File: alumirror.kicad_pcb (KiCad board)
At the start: 2 copper layers, 139.7 x 87.2 mm, 89 parts, among them J1 USB_C_Receptacle_USB2.0_16P_2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, J2 USB_C_Receptacle_USB2.0_16P_2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, J3 USB_C_Receptacle_USB2.0_16P_2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, J4 USB_C_Receptacle_USB2.0_16P_2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, K00 PG1350, K01 PG1350, K02 PG1350, K03 PG1350, K04 PG1350, K05 PG1350, K10 PG1350, K11 PG1350, K12 PG1350, K13 PG1350, K14 PG1350, K15 PG1350, K20 PG1350, K21 PG1350, K22 PG1350, K23 PG1350, K24 PG1350, K25 PG1350_1½U, K30 PG1350_1½U, K31 PG1350/SKQUCAA010, SW1 BOOT, U1 CH552T, U2 CH552T, U3 USBLC6-2P6, U4 USBLC6-2P6, U5 USBLC6-2P6, U6 USBLC6-2P6

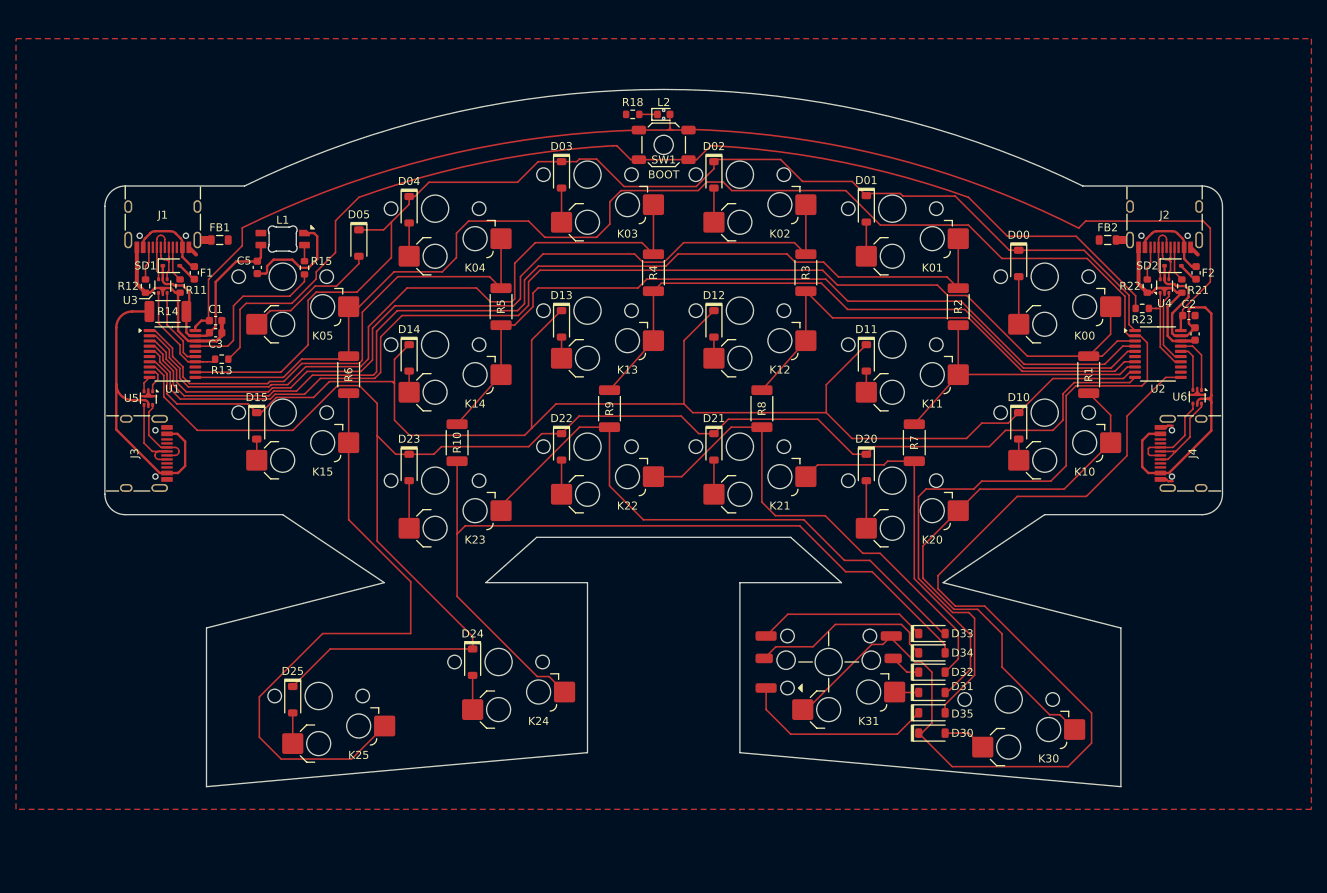
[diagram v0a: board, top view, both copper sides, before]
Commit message: Refine middle layer 3D print cutouts
Also renumber diodes — D0# are now DO# and SD1 and SD2 are and D2
Add diode (D3) on VCC line to RGB LED (this drops VCC to ~4V, which is still within spec., but now closer to the 3.3V control signal as DIN should be VCC±0.5V).
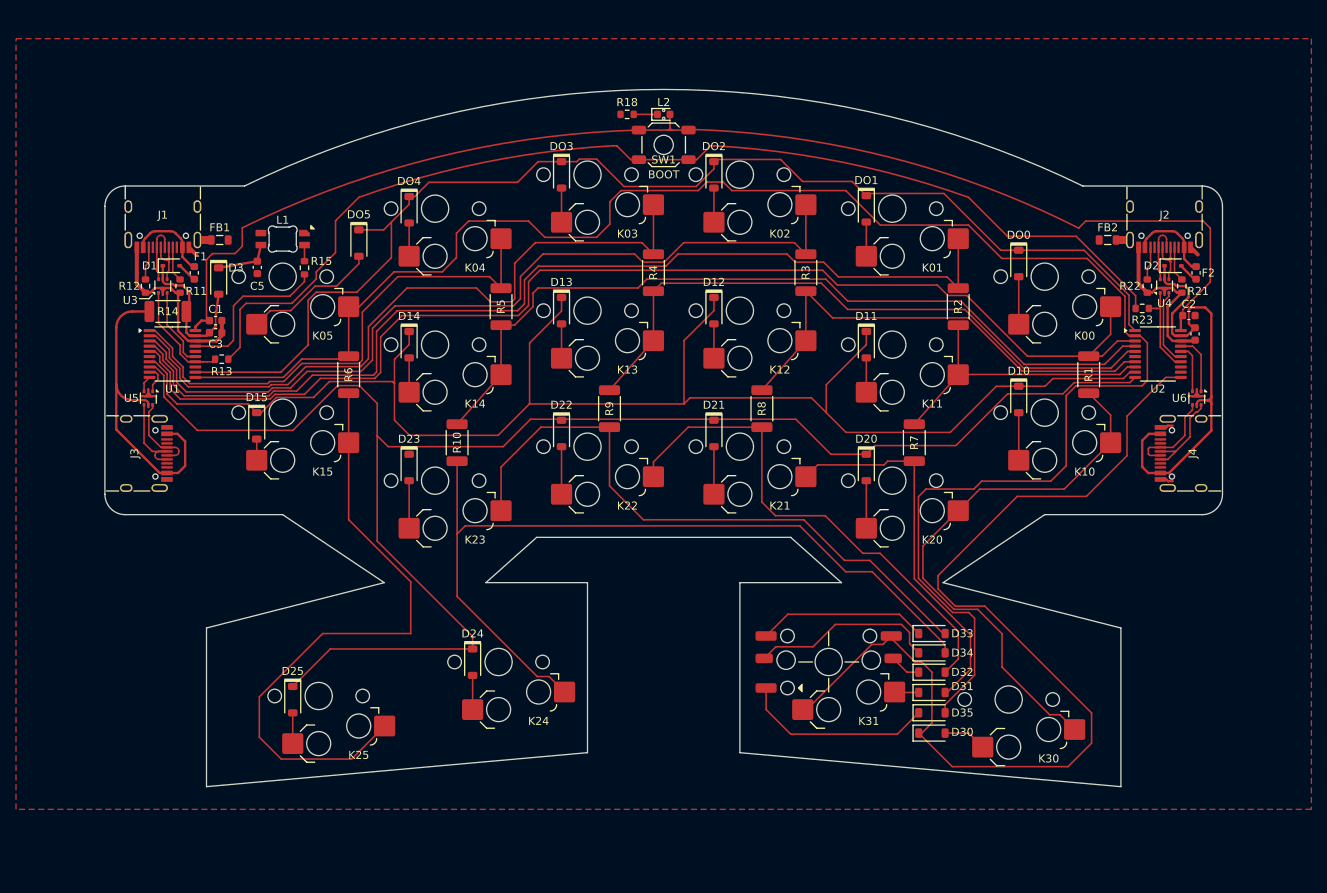
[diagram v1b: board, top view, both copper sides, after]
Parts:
- added D3: 1N4148, Project Library:D_SOD-123_Mod, F.Cu at (96.8, 53.0)
- D30, D31, D32, D33, D34, D35: footprint Project Library:D_SOD-123_Mod -> Diode_SMD:D_SOD-123
- L1: value LED_6028R -> SK6812MINI-E
- R11, R12, R13, R18, R21, R22, R23: footprint Project Library:R_0603_1608Metric_Mod -> Resistor_SMD:R_0603_1608Metric
- R14: footprint Project Library:R_2010_5025Metric_Mod -> Resistor_SMD:R_2010_5025Metric
- R15: value 470 -> 470R; footprint Project Library:R_0603_1608Metric_Mod -> Resistor_SMD:R_0603_1608Metric
- moved D10 3.30 mm to (196.8, 67.8)
- moved D21 1.67 mm to (158.7, 72.0)
- moved D22 1.67 mm to (139.6, 72.0)
- moved D11 1.65 mm to (177.7, 60.9)
- moved D14 1.65 mm to (120.6, 60.9)
- moved D12 1.65 mm to (158.7, 56.7)
- moved D13 1.65 mm to (139.6, 56.7)
- moved R18 0.70 mm to (147.8, 32.1)
- moved U6 0.18 mm to (219.0, 67.6)
- renumbered SD1 to D1, SD2 to D2, D00 to DO0, D01 to DO1, D02 to DO2, D03 to DO3, D04 to DO4, D05 to DO5
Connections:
- C5 pad 1: VCC_L -> Net-(D3-K)
- L1 pad 1: VCC_L -> Net-(D3-K)
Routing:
- net GND: track 65.2 -> 51.0 mm
- net VCC_L: track 28.7 -> 18.7 mm
- net Net-(D3-K): track 0.00 -> 6.96 mm
- net Row2: track 203.8 -> 199.3 mm
- net Row1: track 187.1 -> 190.7 mm
- net Col3RT: track 74.6 -> 78.0 mm
- net Net-(D10-A): track 2.65 -> 5.95 mm
- net +3V3: track 54.6 -> 56.5 mm
- net Net-(D22-A): track 4.28 -> 5.95 mm
- net Net-(D21-A): track 4.28 -> 5.95 mm
- net Net-(D13-A): track 2.65 -> 4.30 mm
- net Net-(D12-A): track 2.65 -> 4.30 mm
- net Net-(D14-A): track 2.65 -> 4.30 mm
- net Net-(D11-A): track 2.65 -> 4.30 mm
- net Col2RT: track 62.5 -> 63.6 mm
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
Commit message: Rotate thumb keys and set outline
Thumb keys rotated by 11° and lined up
Margin around thumb keys is ⅛ vertical U (2.125mm)
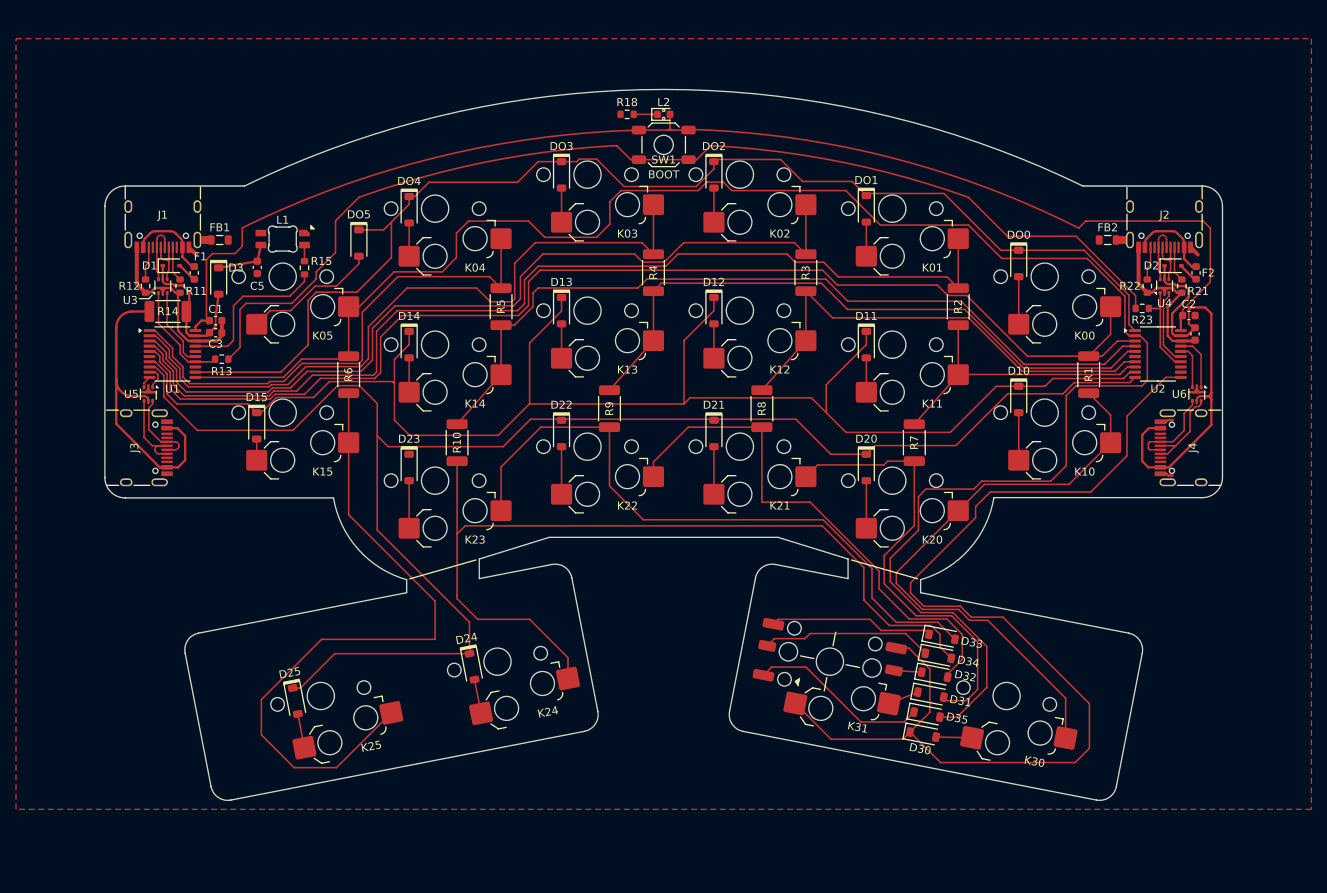
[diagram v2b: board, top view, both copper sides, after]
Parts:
- moved D33 1.33 mm to (187.2, 97.4), turned to -11 degrees
- moved D30 1.13 mm to (184.8, 109.7), turned to -11 degrees
- moved D34 0.88 mm to (186.7, 99.8), turned to -11 degrees
- moved J3 0.71 mm to (86.3, 73.8)
- moved J4 0.71 mm to (218.5, 73.8)
- moved D35 0.67 mm to (185.3, 107.2), turned to -11 degrees
- moved D24 0.56 mm to (128.4, 101.2), turned to -79 degrees
- moved K30 0.51 mm to (195.3, 104.8), turned to -11 degrees
- moved U5 0.50 mm to (88.0, 67.1)
- moved U6 0.50 mm to (219.0, 67.1)
- moved D32 0.47 mm to (186.3, 102.2), turned to -11 degrees
- moved D25 0.36 mm to (106.4, 105.5), turned to -79 degrees
- moved D31 0.31 mm to (185.8, 104.7), turned to -11 degrees
- moved K25 0.26 mm to (109.5, 104.8), turned to 11 degrees
- moved K31 0.16 mm to (173.2, 100.5), turned to -11 degrees
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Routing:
- net Col1RT: track 47.6 -> 56.9 mm
- net Row3R: track 129.6 -> 138.6 mm
- net Col5: track 225.3 -> 232.7 mm
- net Col5T: track 79.0 -> 85.3 mm
- net Col4T: track 103.9 -> 109.2 mm
- net Col0T: track 69.4 -> 74.3 mm
- net Col3RT: track 78.0 -> 81.7 mm
- net Net-(D34-K): track 23.4 -> 21.4 mm
- net Col2RT: track 63.6 -> 65.3 mm
- net Net-(D35-K): track 24.1 -> 22.6 mm
- net Net-(D30-A): track 5.43 -> 4.51 mm
- net Net-(D31-K): track 3.03 -> 3.89 mm
- net Net-(D33-K): track 21.2 -> 20.5 mm
- net VCC_R: track 55.8 -> 55.1 mm
- net TX_R: track 6.14 -> 5.64 mm
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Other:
- board size 139.7 x 87.2 mm -> 139.7 x 88.9 mm

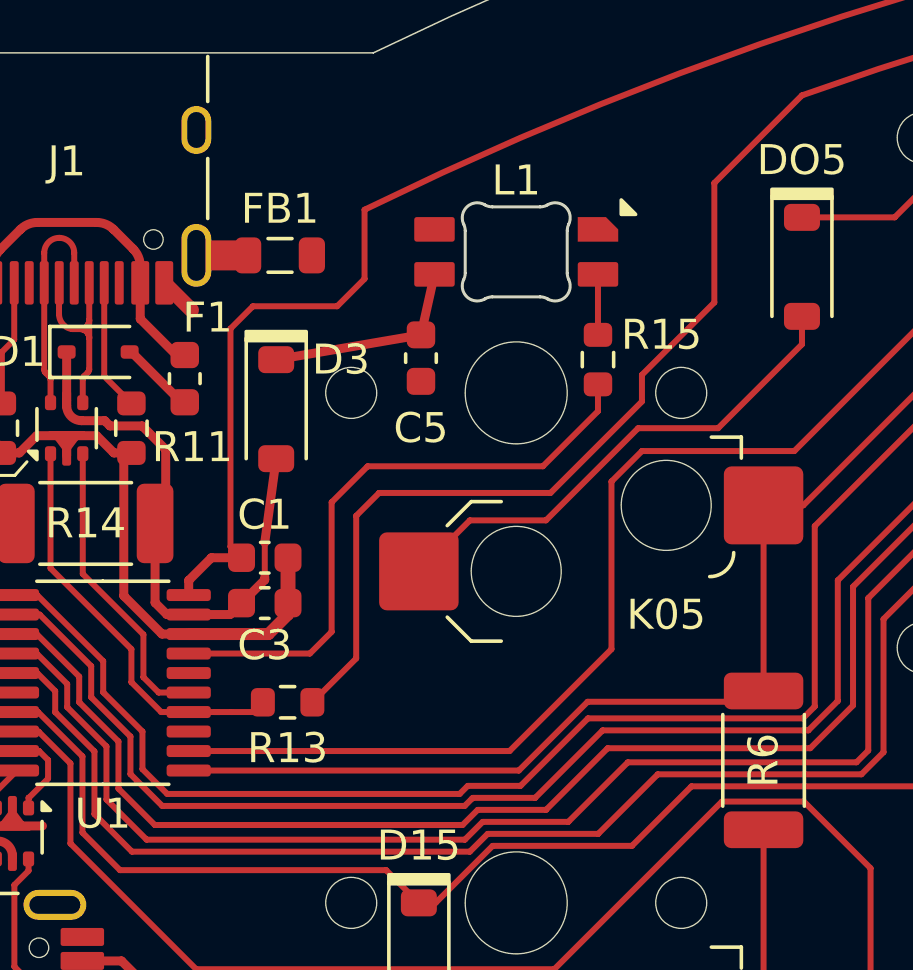
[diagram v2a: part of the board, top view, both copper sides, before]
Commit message: Switch RGB LED capacitor (C5) and resistor (R15) to 0805 size
Found some 0805 470Ω resistors in the parts bin, and this size is a bit less ridiculously small than 0603.
Also, switched LED pin to P1.3 for better spacing and fixed (now) unnecessary misalignment of R13.
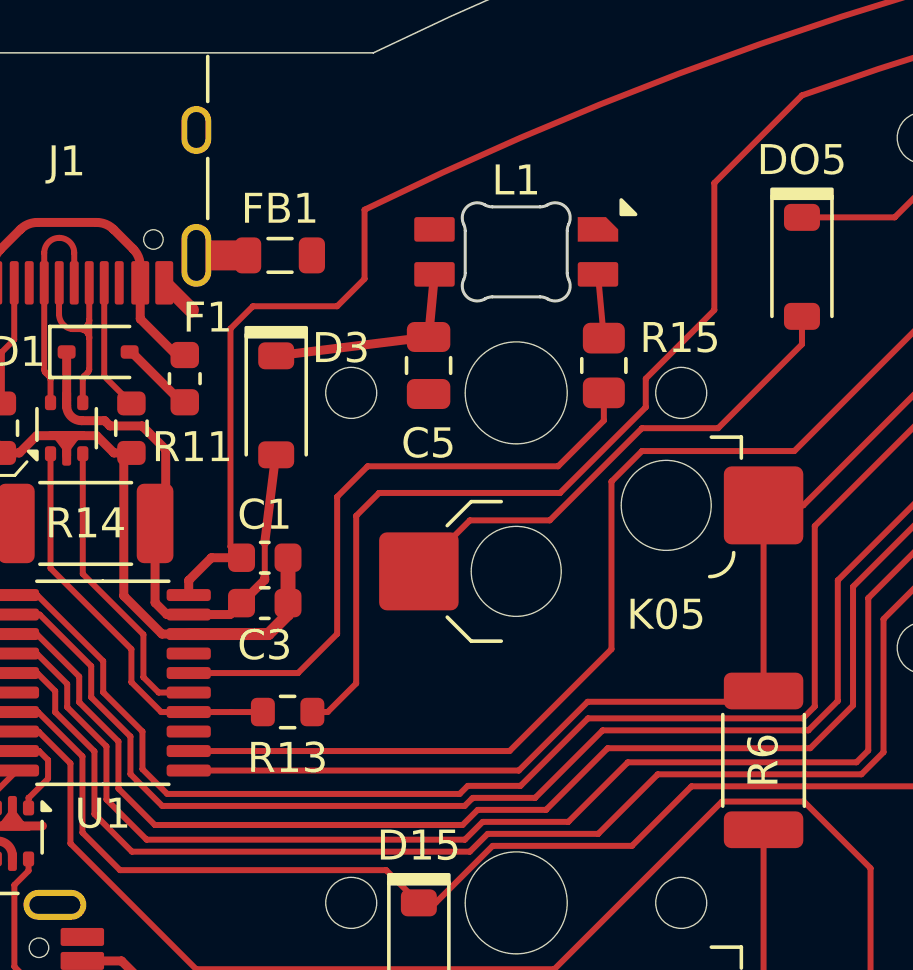
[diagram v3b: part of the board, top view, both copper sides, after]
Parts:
- C5: footprint Capacitor_SMD:C_0603_1608Metric -> Capacitor_SMD:C_0805_2012Metric
- R15: footprint Resistor_SMD:R_0603_1608Metric -> Resistor_SMD:R_0805_2012Metric
- moved C5 0.35 mm to (101.9, 51.5)
- moved R13 0.33 mm to (97.2, 63.1)
- moved R15 0.28 mm to (107.7, 51.5)
- moved D3 0.13 mm to (96.8, 52.8)
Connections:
- U1 pad 16: unconnected-(U1-P1.3-Pad16) -> LED
- U1 pad 17: LED -> unconnected-(U1-P1.2-Pad17)
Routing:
- net BOOT: track 72.0 -> 72.8 mm

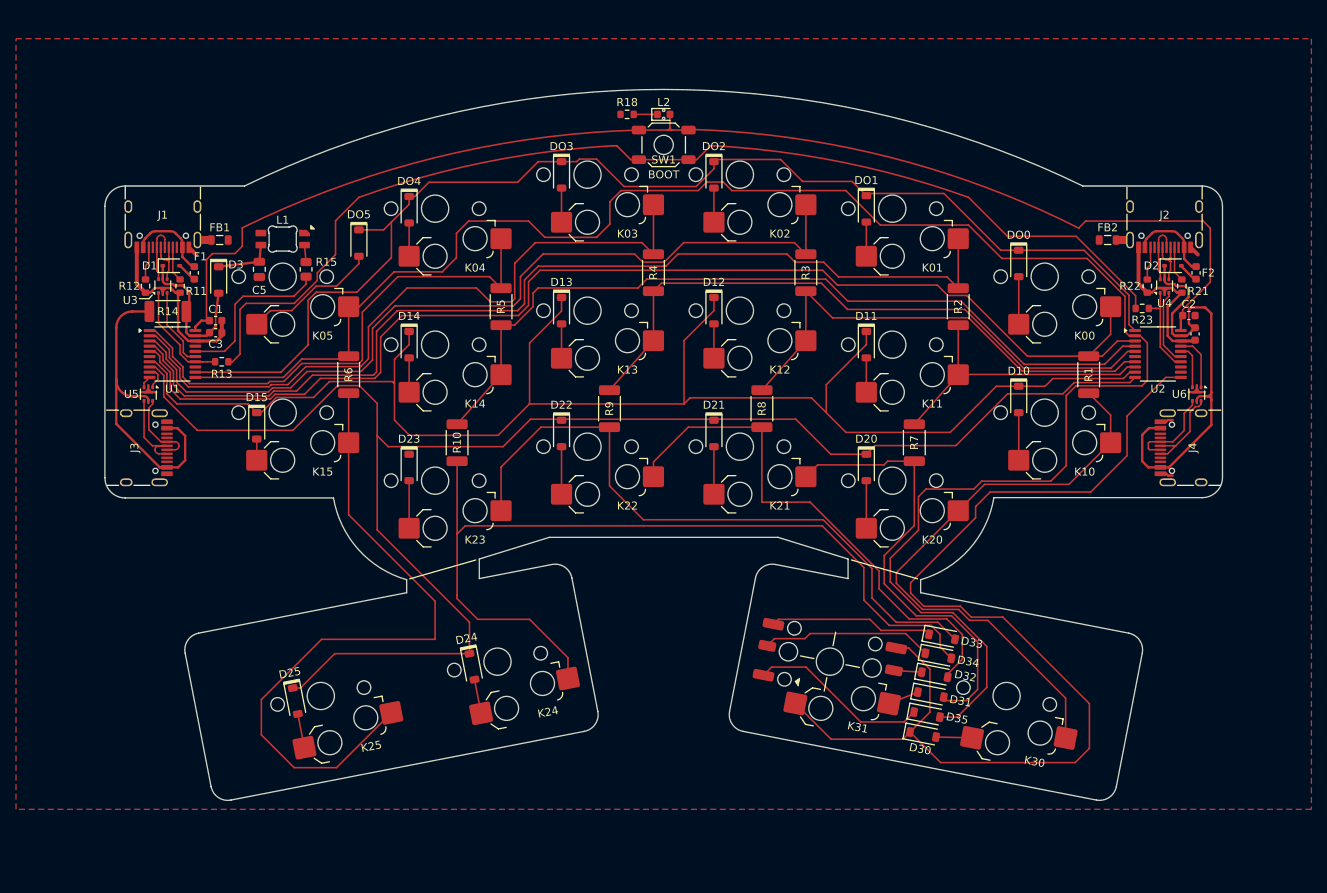
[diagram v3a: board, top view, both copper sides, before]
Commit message: Add mounting holes and re-route tracks around them
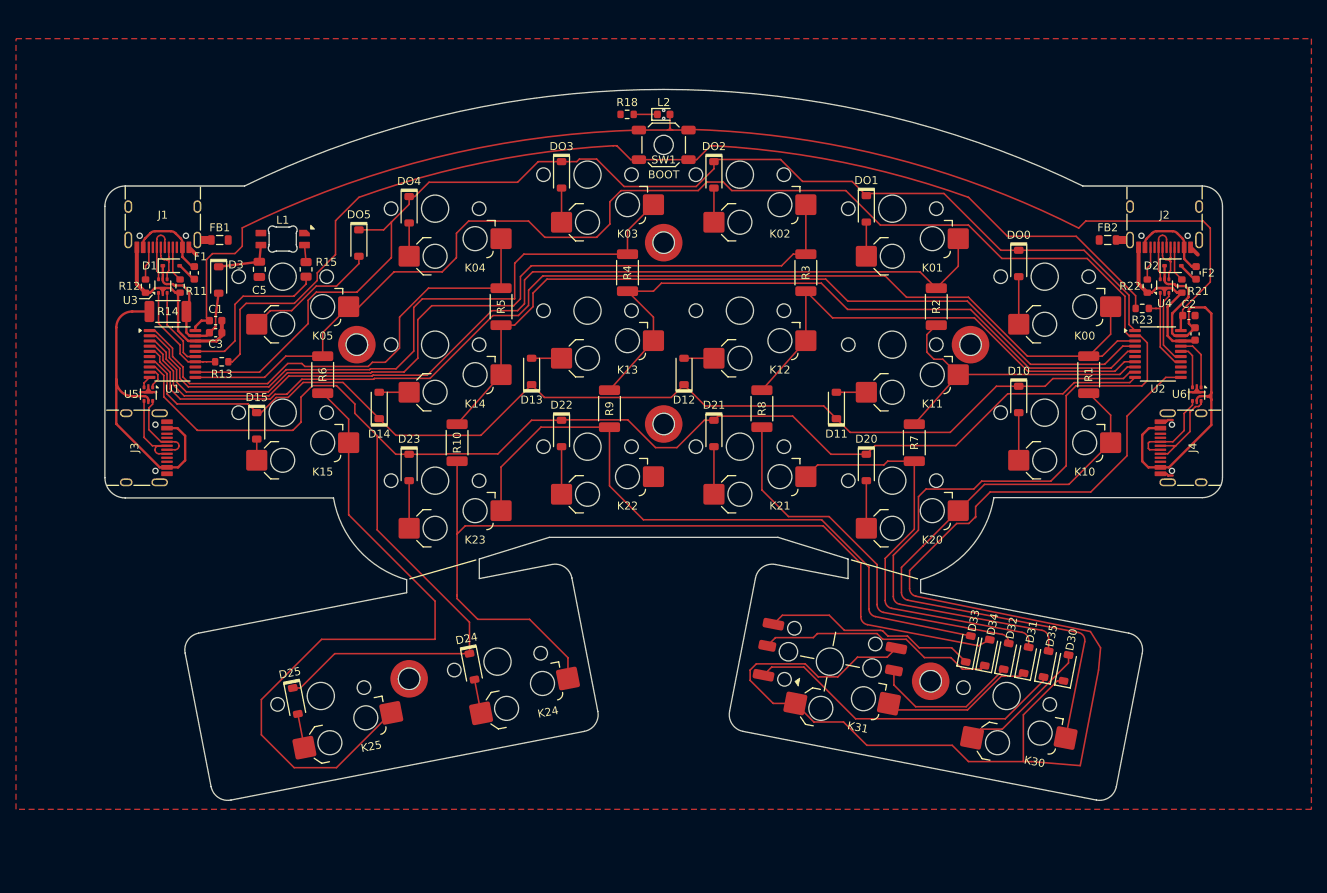
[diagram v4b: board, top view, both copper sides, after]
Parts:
- added H1: MountingHole, Project Library:MountingHole_2.2mm_M2_SMD_Solder_Nut, F.Cu at (114.0, 60.9)
- added H2: MountingHole, Project Library:MountingHole_2.2mm_M2_SMD_Solder_Nut, F.Cu at (152.4, 48.2)
- added H3: MountingHole, Project Library:MountingHole_2.2mm_M2_SMD_Solder_Nut, F.Cu at (152.4, 70.8)
- added H4: MountingHole, Project Library:MountingHole_2.2mm_M2_SMD_Solder_Nut, F.Cu at (190.8, 60.9)
- added H5: MountingHole, Project Library:MountingHole_2.2mm_M2_SMD_Solder_Nut, F.Cu at (120.6, 102.7)
- added H6: MountingHole, Project Library:MountingHole_2.2mm_M2_SMD_Solder_Nut, F.Cu at (185.8, 103.0)
- moved D30 19.7 mm to (202.7, 101.3), turned to 79 degrees
- moved D35 16.2 mm to (200.2, 100.8), turned to 79 degrees
- moved D31 12.7 mm to (197.7, 100.4), turned to 79 degrees
- moved D32 9.23 mm to (195.2, 99.9), turned to 79 degrees
- moved D14 8.47 mm to (116.8, 68.5), turned to 90 degrees
- moved D11 8.47 mm to (174.0, 68.5), turned to 90 degrees
- moved D12 8.47 mm to (154.9, 64.3), turned to 90 degrees
- moved D13 8.47 mm to (135.9, 64.3), turned to 90 degrees
- moved D34 6.12 mm to (192.8, 99.4), turned to 79 degrees
- moved D33 3.61 mm to (190.5, 98.9), turned to 79 degrees
- moved R4 3.25 mm to (147.9, 51.9)
- moved R6 3.24 mm to (109.8, 64.7)
- moved R2 2.75 mm to (186.5, 56.2)
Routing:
- net Row1: track 190.7 -> 141.3 mm
- net Row3R: track 138.6 -> 171.0 mm
- net Net-(D35-K): track 22.6 -> 40.5 mm
- net Col2RT: track 65.3 -> 49.0 mm
- net Net-(D31-K): track 3.89 -> 19.1 mm
- net Net-(D32-K): track 3.48 -> 18.6 mm
- net Net-(D30-A): track 4.51 -> 17.0 mm
- net Net-(D34-K): track 21.4 -> 29.8 mm
- net Net-(D33-K): track 20.5 -> 26.9 mm
- net Col1L: track 125.3 -> 119.0 mm
- net Col0T: track 74.3 -> 79.9 mm
- net Col5: track 232.7 -> 227.5 mm
- net Col3R: track 79.8 -> 84.9 mm
- net Col4T: track 109.2 -> 113.5 mm
- net Row2: track 199.2 -> 203.3 mm
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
